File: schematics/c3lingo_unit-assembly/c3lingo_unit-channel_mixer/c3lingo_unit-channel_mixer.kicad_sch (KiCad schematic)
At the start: 94 parts, among them J301 Interconnect, J302 PowerSupply, J303 I/O, Q301 MMBFJ113, SW301 OnAir_X, SW302 Mute_X, U301 TL072, U302 LM339, U303 LM339, U304 LM339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

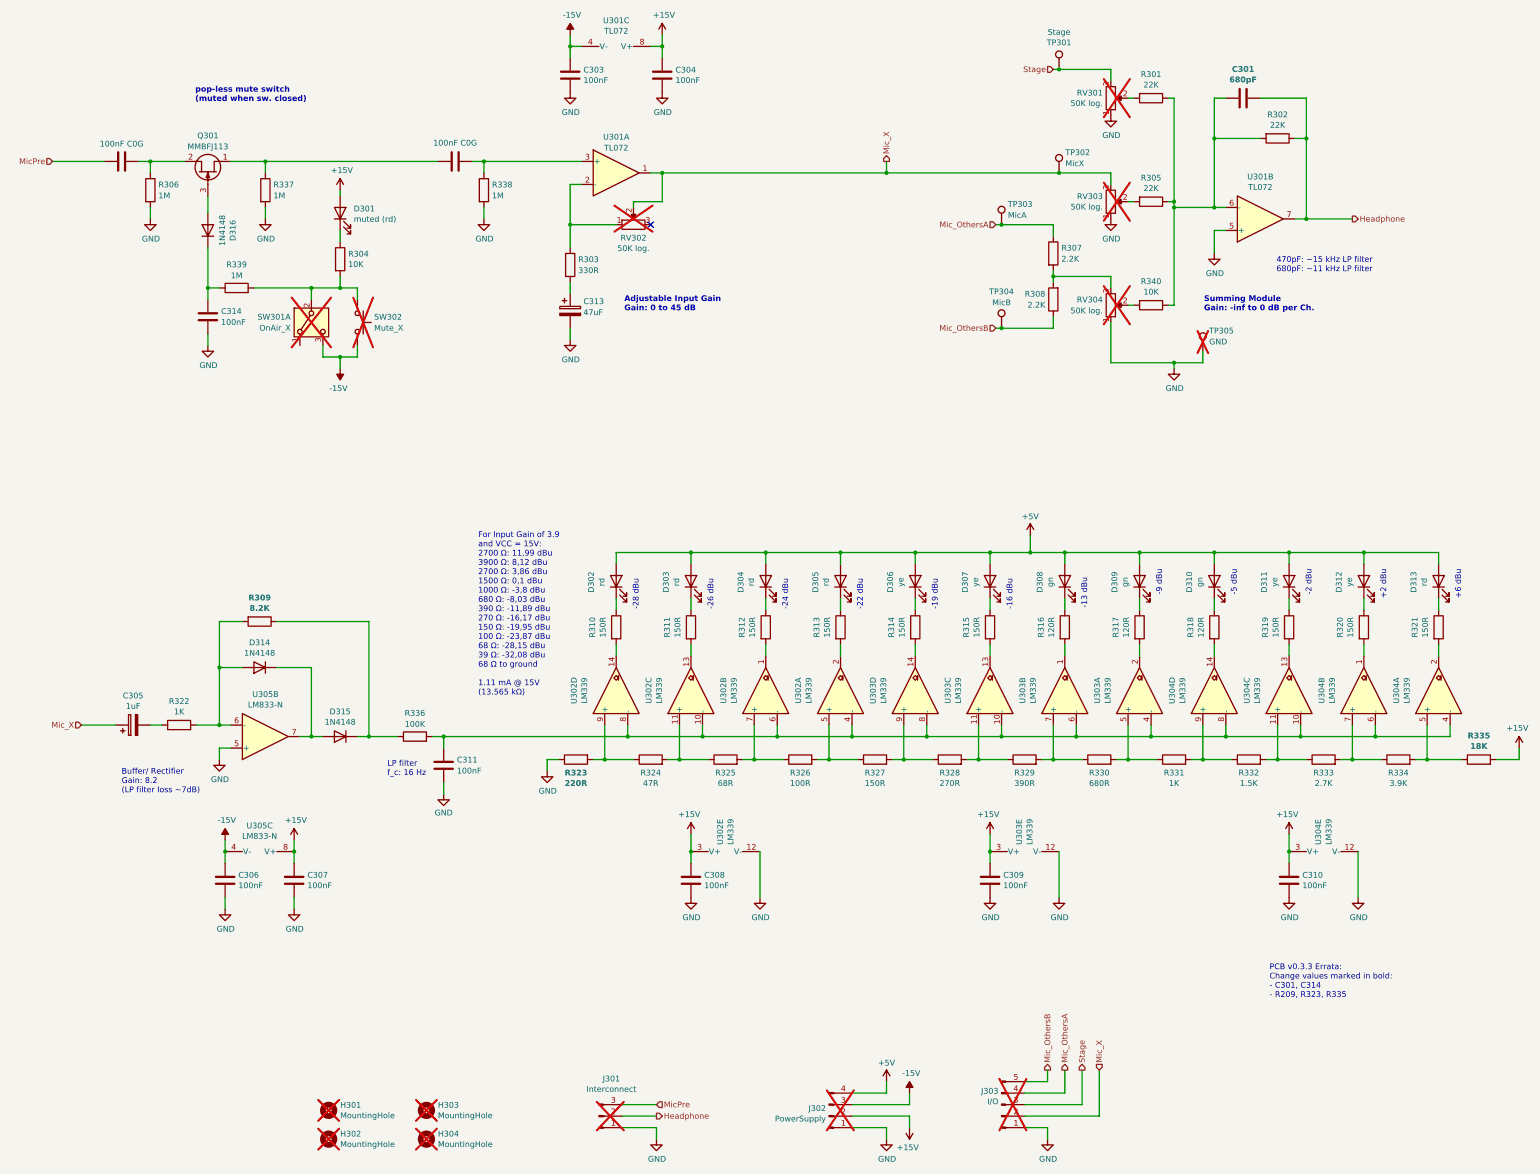
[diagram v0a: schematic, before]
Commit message: Channel Mixer: Reduce mic and output gain
Note: Schematics not re-exported!
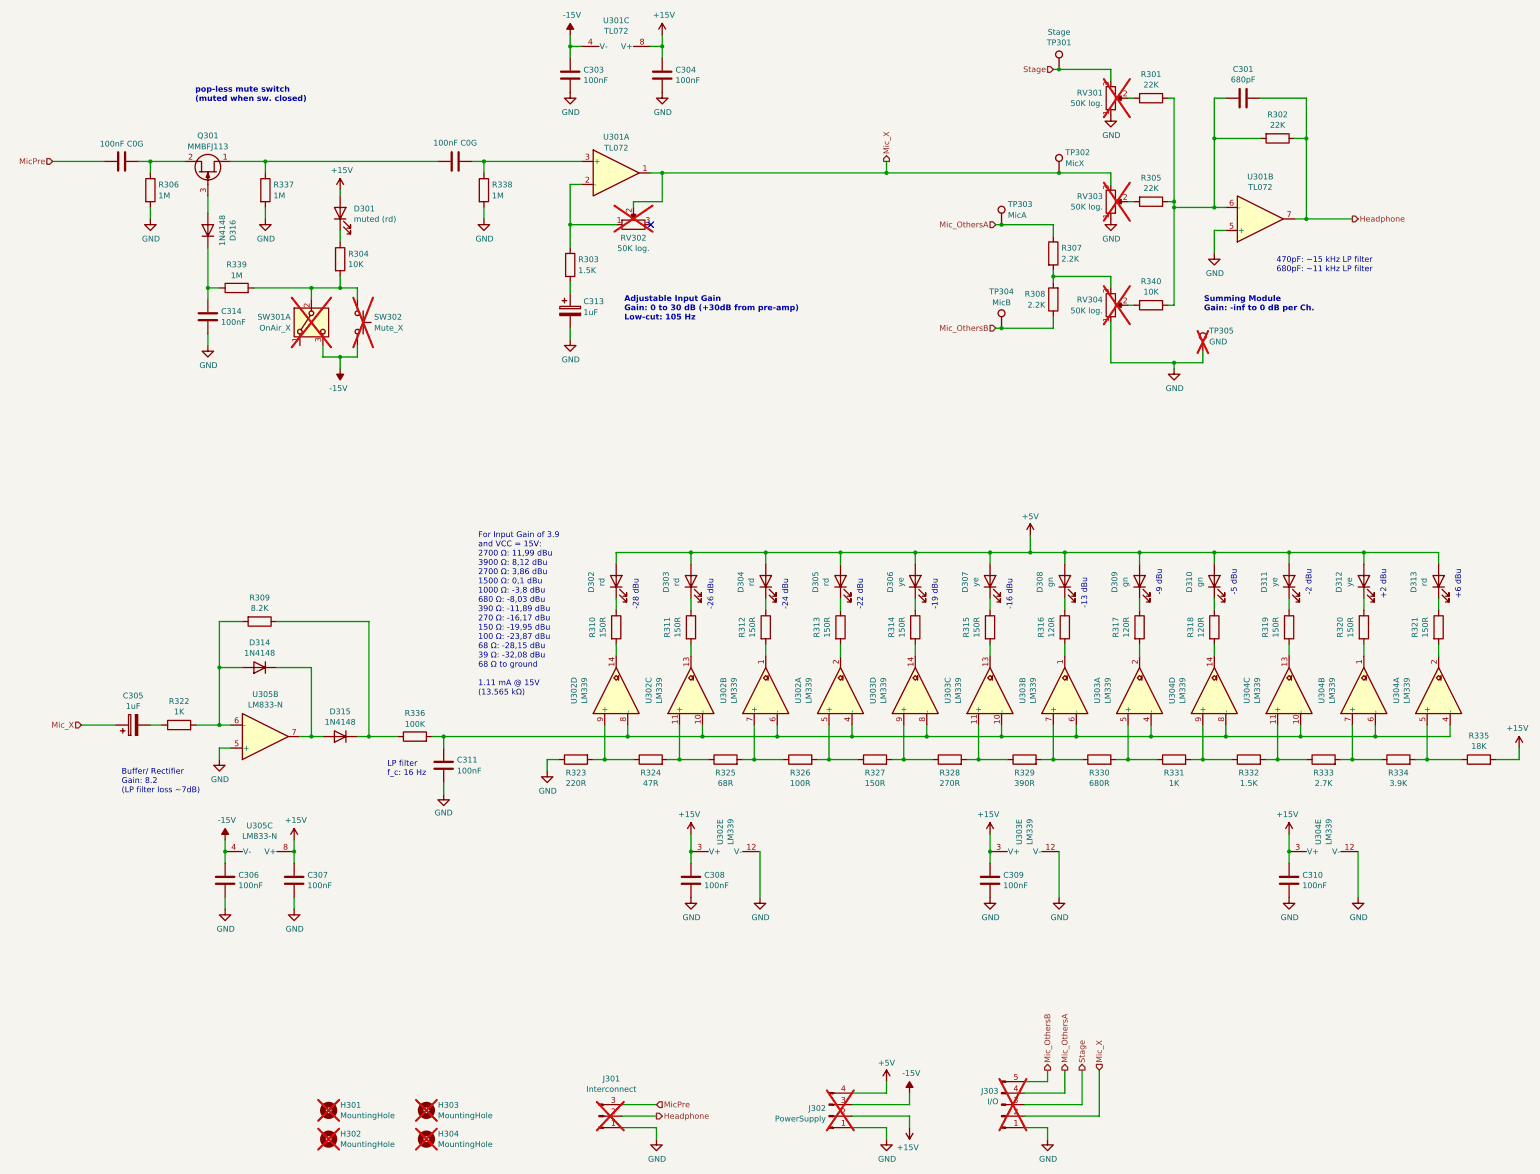
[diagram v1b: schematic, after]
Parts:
- C313: value 47uF -> 1uF; footprint Capacitor_SMD:CP_Elec_6.3x5.4 -> Capacitor_SMD:CP_Elec_4x5.8; LCSC Part # C2836440 -> C336256
- R303: value 330R -> 1.5K
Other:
- note added: "Adjustable Input Gain Gain: 0 to 30 dB (+30dB from pre-amp) Low-cut: 105 Hz"
- note removed: "Adjustable Input Gain Gain: 0 to 45 dB"
- note removed: "PCB v0.3.3 Errata: Change values marked in bold: - C301, C314 - R209, R323, R335"
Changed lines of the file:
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@@
 	(title_block
 		(title "c3lingo interpeter unit -- channel mixer")
-		(date "2024-11-16")
-		(rev "v0.3.4")
+		(date "2024-12-18")
+		(rev "v0.4.0-dev")
 		(company "Jannik Beyerstedt (jtbx)")
-		(comment 1 "Prototype 2 + Rework")
+		(comment 1 "Prototype 3")
 	)
 	(junction
@@
 		)
 	)
-	(text "Adjustable Input Gain\nGain: 0 to 45 dB"
+	(text "Adjustable Input Gain\nGain: 0 to 30 dB (+30dB from pre-amp)\nLow-cut: 105 Hz"
 		(exclude_from_sim no)
-		(at 157.988 96.774 0)
+		(at 157.988 98.806 0)
 		(effects
 			(font
@@
 		)
 	)
-	(text "PCB v0.3.3 Errata:\nChange values marked in bold:\n- C301, C314\n- R209, R323, R335"
-		(exclude_from_sim no)
-		(at 300.482 244.602 0)
-		(effects
-			(font
-				(size 1.27 1.27)
-			)
-			(justify left)
-		)
-	)
 	(text "-5 dBu"
 		(exclude_from_sim no)
@@
 		(shape output)
 		(at 251.46 264.16 90)
-		(fields_autoplaced yes)
 		(effects
 			(font
@@
 		(shape input)
 		(at 165.1 271.78 0)
-		(fields_autoplaced yes)
 		(effects
 			(font
@@
 		(shape input)
 		(at 38.1 187.96 180)
-		(fields_autoplaced yes)
 		(effects
 			(font
@@
 		(shape input)
 		(at 252.73 43.18 180)
-		(fields_autoplaced yes)
 		(effects
 			(font
@@
 		(shape output)
 		(at 165.1 274.32 0)
-		(fields_autoplaced yes)
 		(effects
 			(font
@@
 		(shape output)
 		(at 255.27 264.16 90)
-		(fields_autoplaced yes)
 		(effects
 			(font
@@
 		(shape input)
 		(at 31.75 63.5 180)
-		(fields_autoplaced yes)
 		(effects
 			(font
@@
 		(shape input)
 		(at 240.03 100.33 180)
-		(fields_autoplaced yes)
 		(effects
 			(font
@@
 		(shape input)
 		(at 240.03 77.47 180)
-		(fields_autoplaced yes)
 		(effects
 			(font
@@
 		(shape output)
 		(at 318.77 76.2 0)
-		(fields_autoplaced yes)
 		(effects
 			(font
@@
 		(shape output)
 		(at 215.9 63.5 90)
-		(fields_autoplaced yes)
 		(effects
 			(font
@@
 		(shape output)
 		(at 259.08 264.16 90)
-		(fields_autoplaced yes)
 		(effects
 			(font
@@
 		(shape input)
 		(at 262.89 264.16 90)
-		(fields_autoplaced yes)
 		(effects
 			(font
@@
 				(font
 					(size 1.27 1.27)
-					(thickness 0.254)
-					(bold yes)
+					(thickness 0.1588)
 				)
 			)
@@
 				(font
 					(size 1.27 1.27)
-					(thickness 0.254)
-					(bold yes)
+					(thickness 0.1588)
 				)
 			)
@@
 			)
 		)
-		(property "Value" "330R"
+		(property "Value" "1.5K"
 			(at 147.828 87.5721 0)
 			(effects
@@
 				(font
 					(size 1.27 1.27)
-					(thickness 0.254)
-					(bold yes)
+					(thickness 0.1588)
 				)
 			)
@@
 				(font
 					(size 1.27 1.27)
-					(thickness 0.254)
-					(bold yes)
+					(thickness 0.1588)
 				)
 			)
@@
 				(font
 					(size 1.27 1.27)
-					(thickness 0.254)
-					(bold yes)
+					(thickness 0.1588)
 				)
 			)
@@
 				(font
 					(size 1.27 1.27)
-					(thickness 0.254)
-					(bold yes)
+					(thickness 0.1588)
 				)
 			)
@@
 				(font
 					(size 1.27 1.27)
-					(thickness 0.254)
-					(bold yes)
+					(thickness 0.1588)
 				)
 			)
@@
 				(font
 					(size 1.27 1.27)
-					(thickness 0.254)
-					(bold yes)
+					(thickness 0.1588)
 				)
 			)
@@
 			)
 		)
-		(property "Value" "47uF"
+		(property "Value" "1uF"
 			(at 148.971 96.8431 0)
 			(effects
@@
 			)
 		)
-		(property "Footprint" "Capacitor_SMD:CP_Elec_6.3x5.4"
+		(property "Footprint" "Capacitor_SMD:CP_Elec_4x5.8"
 			(at 147.0152 100.33 0)
 			(effects
@@
 			)
 		)
-		(property "LCSC Part #" "C2836440"
+		(property "LCSC Part #" "C336256"
 			(at 146.05 96.52 0)
 			(effects

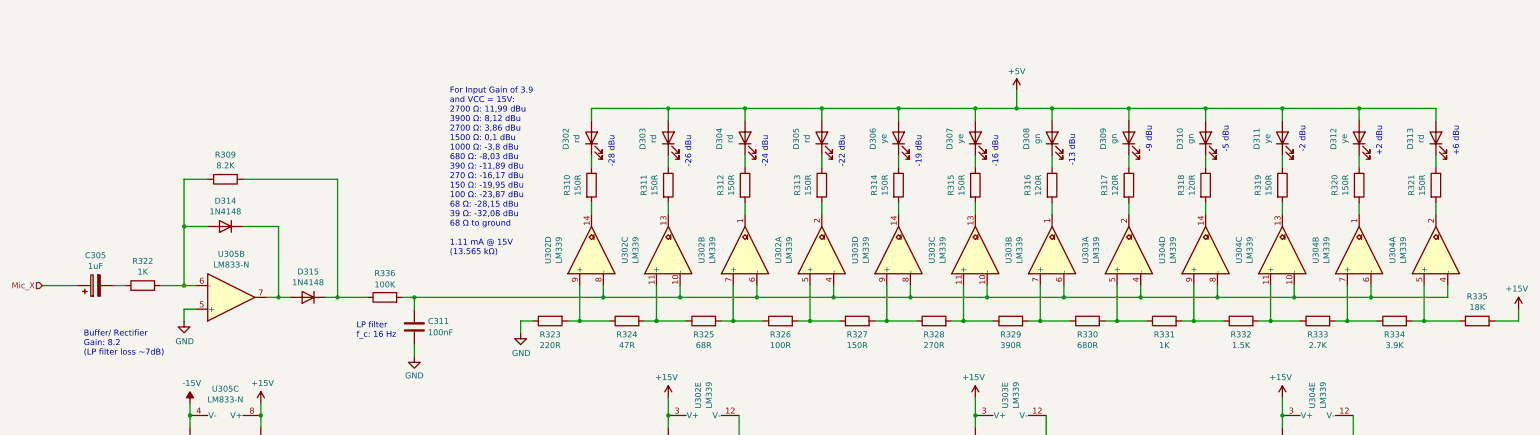
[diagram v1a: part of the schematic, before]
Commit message: Channel Mixer: Re-design VU meter scale
Note: Schematic not re-exported!
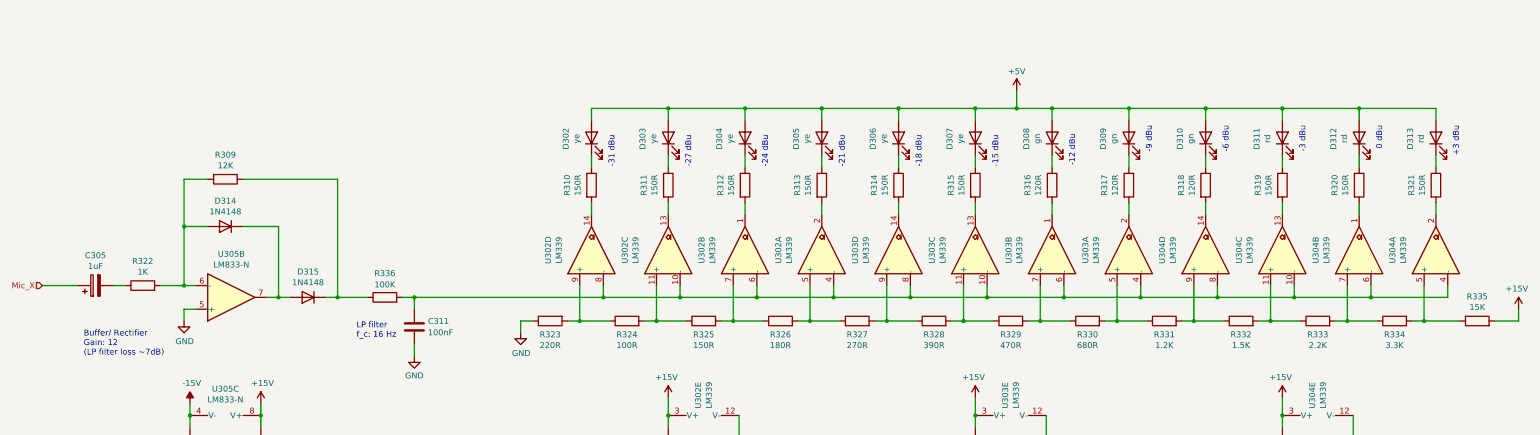
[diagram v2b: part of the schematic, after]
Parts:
- D302, D303, D304, D305: value rd -> ye; LCSC Part # C84256 -> C2296; Model generic 20 mA, 2.0 V -> generic 20 mA, 2.1 V
- D311, D312: value ye -> rd; LCSC Part # C2296 -> C84256; Model generic 20 mA, 2.1 V -> generic 20 mA, 2.0 V
- R309: value 8.2K -> 12K
- R324: value 47R -> 100R
- R325: value 68R -> 150R
- R326: value 100R -> 180R
- R327: value 150R -> 270R
- R328: value 270R -> 390R
- R329: value 390R -> 470R
- R331: value 1K -> 1.2K
- R333: value 2.7K -> 2.2K
- R334: value 3.9K -> 3.3K
- R335: value 18K -> 15K
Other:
- note added: "+3 dBu"
- note added: "-12 dBu"
- note added: "-15 dBu"
- note added: "-18 dBu"
- note added: "-21 dBu"
- note added: "-27 dBu"
- note added: "-3 dBu"
- note added: "-31 dBu"
- note added: "-6 dBu"
- note added: "0 dBu"
- note added: "Buffer/ Rectifier Gain: 12 (LP filter loss ~7dB)"
- note removed: "+2 dBu"
- note removed: "+6 dBu"
- note removed: "-13 dBu"
- note removed: "-16 dBu"
- note removed: "-19 dBu"
- note removed: "-2 dBu"
- note removed: "-22 dBu"
- note removed: "-26 dBu"
- note removed: "-28 dBu"
- note removed: "-5 dBu"
- note removed: "Buffer/ Rectifier Gain: 8.2 (LP filter loss ~7dB)"
- note removed: "For Input Gain of 3.9 and VCC = 15V: 2700 Ω: 11,99 dBu 3900 Ω: 8,12 dBu 2700 Ω: 3,86 dBu 1500 Ω: 0,1 dBu 1000 Ω: -3,8 dBu 680 Ω: -8,03 dBu 390 Ω: -11,89 dBu 270 Ω: -16,17 dBu 150 Ω: -19,95 dBu 100 Ω: -23,87 dBu 68 Ω: -28,15 dBu 39 Ω: -32,08 dBu 68 Ω to ground 1.11 mA @ 15V (13.565 kΩ)"
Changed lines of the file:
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@@
 		)
 	)
-	(text "-19 dBu"
+	(text "-18 dBu"
 		(exclude_from_sim no)
 		(at 227.33 162.56 90)
@@
 		)
 	)
-	(text "-22 dBu"
+	(text "-21 dBu"
 		(exclude_from_sim no)
 		(at 210.82 162.56 90)
@@
 		)
 	)
-	(text "-2 dBu"
+	(text "-3 dBu"
 		(exclude_from_sim no)
 		(at 309.88 153.67 90)
@@
 		)
 	)
-	(text "+2 dBu"
+	(text "0 dBu"
 		(exclude_from_sim no)
 		(at 326.39 153.67 90)
@@
 		)
 	)
-	(text "For Input Gain of 3.9\nand VCC = 15V:\n2700 Ω: 11,99 dBu\n3900 Ω: 8,12 dBu\n2700 Ω: 3,86 dBu\n1500 Ω: 0,1 dBu\n1000 Ω: -3,8 dBu\n680 Ω: -8,03 dBu\n390 Ω: -11,89 dBu\n270 Ω: -16,17 dBu\n150 Ω: -19,95 dBu\n100 Ω: -23,87 dBu\n68 Ω: -28,15 dBu\n39 Ω: -32,08 dBu\n68 Ω to ground\n\n1.11 mA @ 15V\n(13.565 kΩ)"
-		(exclude_from_sim no)
-		(at 125.73 181.61 0)
-		(effects
-			(font
-				(size 1.27 1.27)
-			)
-			(justify left bottom)
-		)
-	)
-	(text "+6 dBu"
+	(text "+3 dBu"
 		(exclude_from_sim no)
 		(at 342.9 153.67 90)
@@
 		)
 	)
-	(text "-16 dBu"
+	(text "-15 dBu"
 		(exclude_from_sim no)
 		(at 243.84 162.56 90)
@@
 		)
 	)
-	(text "-13 dBu"
+	(text "-12 dBu"
 		(exclude_from_sim no)
 		(at 260.35 162.306 90)
@@
 		)
 	)
-	(text "-28 dBu"
+	(text "-31 dBu"
 		(exclude_from_sim no)
 		(at 161.29 162.56 90)
@@
 		)
 	)
-	(text "-26 dBu"
+	(text "-27 dBu"
 		(exclude_from_sim no)
 		(at 177.8 162.56 90)
@@
 		)
 	)
-	(text "-5 dBu"
+	(text "-6 dBu"
 		(exclude_from_sim no)
 		(at 293.37 153.67 90)
@@
 		)
 	)
-	(text "Buffer/ Rectifier\nGain: 8.2\n(LP filter loss ~7dB)"
+	(text "Buffer/ Rectifier\nGain: 12\n(LP filter loss ~7dB)"
 		(exclude_from_sim no)
 		(at 46.99 203.2 0)
@@
 			)
 		)
-		(property "Value" "3.9K"
+		(property "Value" "3.3K"
 			(at 328.93 200.8124 90)
 			(effects
@@
 			)
 		)
-		(property "Value" "1K"
+		(property "Value" "1.2K"
 			(at 279.4 200.8124 90)
 			(effects
@@
 			)
 		)
-		(property "Value" "2.7K"
+		(property "Value" "2.2K"
 			(at 312.42 200.8124 90)
 			(effects
@@
 			)
 		)
-		(property "Value" "150R"
+		(property "Value" "270R"
 			(at 213.36 200.8124 90)
 			(effects
@@
 			)
 		)
-		(property "Value" "390R"
+		(property "Value" "470R"
 			(at 246.38 200.8124 90)
 			(effects
@@
 			)
 		)
-		(property "Value" "270R"
+		(property "Value" "390R"
 			(at 229.87 200.8124 90)
 			(effects
@@
 			)
 		)
-		(property "Value" "100R"
+		(property "Value" "180R"
 			(at 196.85 200.8124 90)
 			(effects
@@
 			)
 		)
-		(property "Value" "68R"
+		(property "Value" "150R"
 			(at 180.34 200.8124 90)
 			(effects
@@
 			)
 		)
-		(property "Value" "47R"
+		(property "Value" "100R"
 			(at 163.83 200.8124 90)
 			(effects
@@
 			)
 		)
-		(property "Value" "ye"
+		(property "Value" "rd"
 			(at 318.1096 156.3878 0)
 			(effects
@@
 			)
 		)
-		(property "Description" "needs 145R @5V"
+		(property "Description" "needs 150R @5V"
 			(at 321.31 156.21 0)
 			(effects
@@
 			)
 		)
-		(property "Model" "generic 20 mA, 2.1 V"
+		(property "Model" "generic 20 mA, 2.0 V"
 			(at 321.31 156.21 0)
 			(effects
@@
 			)
 		)
-		(property "LCSC Part #" "C2296"
+		(property "LCSC Part #" "C84256"
 			(at 321.31 156.21 0)
 			(effects
@@
 			)
 		)
-		(property "Value" "ye"
+		(property "Value" "rd"
 			(at 301.5996 156.3878 0)
 			(effects
@@
 			)
 		)
-		(property "Description" "needs 145R @5V"
+		(property "Description" "needs 150R @5V"
 			(at 304.8 156.21 0)
 			(effects
@@
 			)
 		)
-		(property "Model" "generic 20 mA, 2.1 V"
+		(property "Model" "generic 20 mA, 2.0 V"
 			(at 304.8 156.21 0)
 			(effects
@@
 			)
 		)
-		(property "LCSC Part #" "C2296"
+		(property "LCSC Part #" "C84256"
 			(at 304.8 156.21 0)
 			(effects
@@
 			)
 		)
-		(property "Value" "rd"
+		(property "Value" "ye"
 			(at 202.5396 156.3878 0)
 			(effects
@@
 			)
 		)
-		(property "Description" "needs 150R @5V"
+		(property "Description" "needs 145R @5V"
 			(at 205.74 156.21 0)
 			(effects
@@
 			)
 		)
-		(property "Model" "generic 20 mA, 2.0 V"
+		(property "Model" "generic 20 mA, 2.1 V"
 			(at 205.74 156.21 0)
 			(effects
@@
 			)
 		)
-		(property "LCSC Part #" "C84256"
+		(property "LCSC Part #" "C2296"
 			(at 205.74 156.21 0)
 			(effects
@@
 			)
 		)
-		(property "Value" "rd"
+		(property "Value" "ye"
 			(at 186.0296 156.3878 0)
 			(effects
@@
 			)
 		)
-		(property "Description" "needs 150R @5V"
+		(property "Description" "needs 145R @5V"
 			(at 189.23 156.21 0)
 			(effects
@@
 			)
 		)
-		(property "Model" "generic 20 mA, 2.0 V"
+		(property "Model" "generic 20 mA, 2.1 V"
 			(at 189.23 156.21 0)
 			(effects
@@
 			)
 		)
-		(property "LCSC Part #" "C84256"
+		(property "LCSC Part #" "C2296"
 			(at 189.23 156.21 0)
 			(effects
@@
 			)
 		)
-		(property "Value" "rd"
+		(property "Value" "ye"
 			(at 169.5196 156.3878 0)
 			(effects
@@
 			)
 		)
-		(property "Description" "needs 150R @5V"
+		(property "Description" "needs 145R @5V"
 			(at 172.72 156.21 0)
 			(effects
@@
 			)
 		)
-		(property "Model" "generic 20 mA, 2.0 V"
+		(property "Model" "generic 20 mA, 2.1 V"
 			(at 172.72 156.21 0)
 			(effects
@@
 			)
 		)
-		(property "LCSC Part #" "C84256"
+		(property "LCSC Part #" "C2296"
 			(at 172.72 156.21 0)
 			(effects
@@
 			)
 		)
-		(property "Value" "rd"
+		(property "Value" "ye"
 			(at 153.0096 156.3878 0)
 			(effects
@@
 			)
 		)
-		(property "Description" "needs 150R @5V"
+		(property "Description" "needs 145R @5V"
 			(at 156.21 156.21 0)
 			(effects
@@
 			)
 		)
-		(property "Model" "generic 20 mA, 2.0 V"
+		(property "Model" "generic 20 mA, 2.1 V"
 			(at 156.21 156.21 0)
 			(effects
@@
 			)
 		)
-		(property "LCSC Part #" "C84256"
+		(property "LCSC Part #" "C2296"
 			(at 156.21 156.21 0)
 			(effects
@@
 			)
 		)
-		(property "Value" "8.2K"
+		(property "Value" "12K"
 			(at 77.47 162.1536 90)
 			(effects
@@
 			)
 		)
-		(property "Value" "18K"
+		(property "Value" "15K"
 			(at 346.71 192.6336 90)
 			(effects
